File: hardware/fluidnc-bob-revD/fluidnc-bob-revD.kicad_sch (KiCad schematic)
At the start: 69 parts, among them J1 36V-IN, J10 RELAY, J11 AUX, J12 5V-EXT, J13 SD, J2 X-DRV, J3 Y-DRV, J4 Z-DRV, J5 LIM-X, J6 LIM-Y, J7 LIM-Z, J8 PROBE, J9 E-STOP, Q1 MMBT2222A, Q2 MMBT2222A, U1 SN74AHCT541N, U2 TSR 1-4850WI

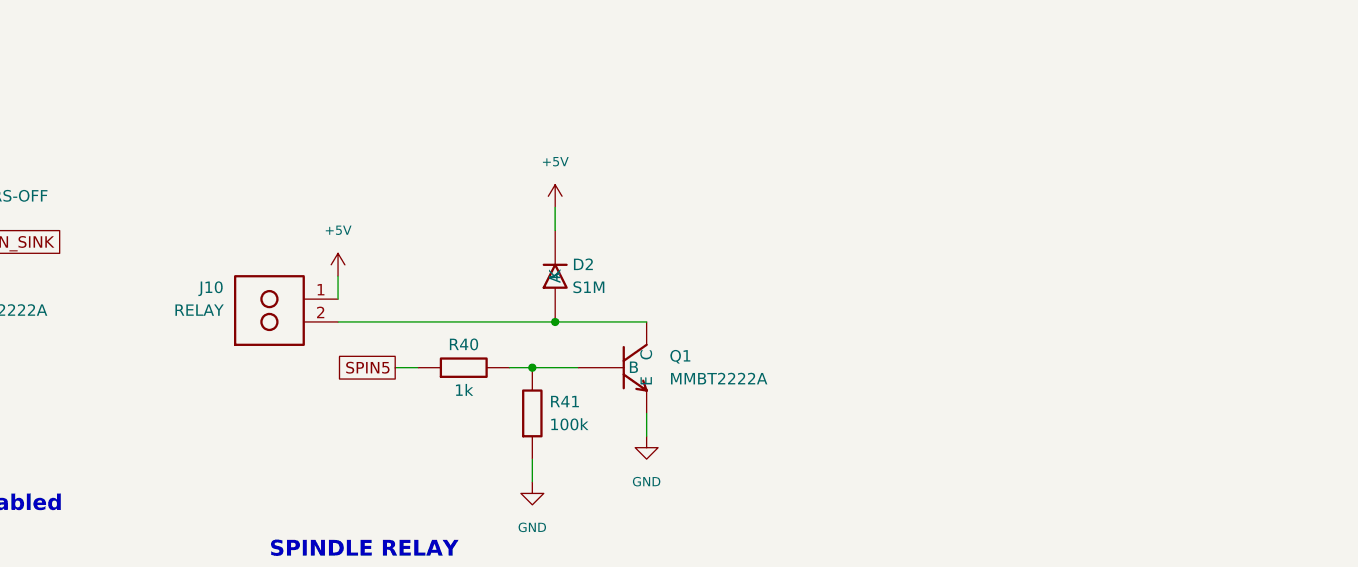
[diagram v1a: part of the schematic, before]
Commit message: hardware: rev D — onboard spindle relay (Omron G5LE-14 DC5)
Replaces the harvest-a-Songle off-board plan: G5LE-14 DC5 (SPDT,
10A/250VAC, 5V coil, DK Z1011-ND) driven by the existing Q1 low-side
sink + S1M flyback. Contacts COM/NO/NC to a 3-pos MKDS terminal (J10,
Phoenix 1715734) switching the spindle AC line — wire through NO so a
dead board fails spindle-off. Pin map (coil 2&5, COM 1, NO 3, NC 4)
decoded from the Omron datasheet + KiCad curated footprint.

verify_netlist caught a COM-to-NO short in the first contact routing
(polyline vertex landing on a terminal pin tip) — rerouted on distinct
lanes. ERC 0 violations; netlist verified. BOM/CSV/README updated,
mains creepage rules added to the layout checklist.

Co-Authored-By: Claude Fable 5 <noreply@anthropic.com>
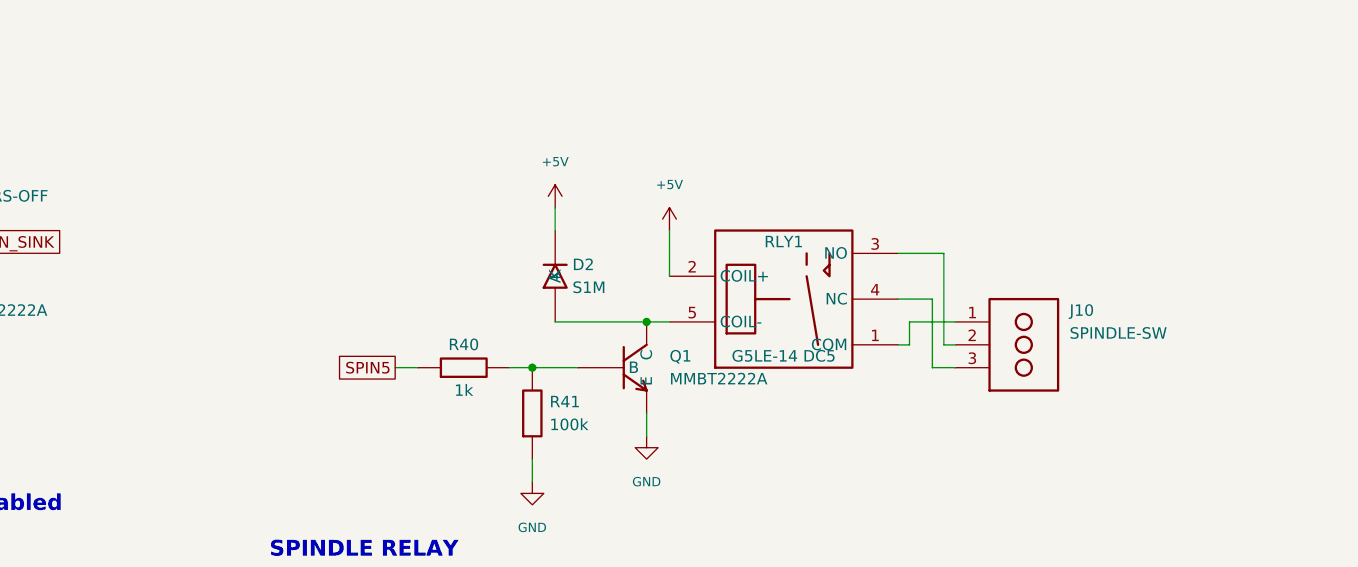
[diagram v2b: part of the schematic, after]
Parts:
- removed J10: RELAY, TerminalBlock_Phoenix:TerminalBlock_Phoenix_MKDS-1,5-2-5.08_1x02_P5.08mm_Horizontal, symbol bobD:TB_02
- added J10: SPINDLE-SW, TerminalBlock_Phoenix:TerminalBlock_Phoenix_MKDS-1,5-3-5.08_1x03_P5.08mm_Horizontal, symbol bobD:TB_03L
- added RLY1: G5LE-14 DC5, Relay_THT:Relay_SPDT_Omron-G5LE-1, symbol bobD:RELAY_G5LE
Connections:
- net +5V: now also RLY1.2 (COIL+)
- net at D2.2 (A), Q1.3 (C): now also RLY1.5 (COIL-)
- new net: J10.1, RLY1.1 (COM)
- new net: J10.2, RLY1.3 (NO)
- new net: J10.3, RLY1.4 (NC)
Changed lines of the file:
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@@
     (instances (project "fluidnc-bob-revD" (path "/d27f0a00-3830-5100-af6a-a93fbdba8465" (reference "D2") (unit 1))))
   )
-  (symbol (lib_id "bobD:TB_02") (at 158.75 220.98 0) (unit 1) (exclude_from_sim no) (in_bom yes) (on_board yes) (dnp no)
-    (property "Reference" "J10" (at 153.67 219.70999999999998 0) (effects (font (size 1.27 1.27)) (justify right)))
-    (property "Value" "RELAY" (at 153.67 222.25 0) (effects (font (size 1.27 1.27)) (justify right)))
-    (property "Footprint" "TerminalBlock_Phoenix:TerminalBlock_Phoenix_MKDS-1,5-2-5.08_1x02_P5.08mm_Horizontal" (at 158.75 220.98 0) (effects (font (size 1.27 1.27)) hide))
-    (property "Datasheet" "https://www.phoenixcontact.com/en-us/products/printed-circuit-board-terminal-mkds-15-2-508-1715721" (at 158.75 220.98 0) (effects (font (size 1.27 1.27)) hide))
-    (property "Digikey" "https://www.digikey.com/en/products/detail/phoenix-contact/1715721/260631" (at 158.75 220.98 0) (effects (font (size 1.27 1.27)) hide))
-    (pin "1")
+  (symbol (lib_id "bobD:RELAY_G5LE") (at 215.9 220.98 0) (unit 1) (exclude_from_sim no) (in_bom yes) (on_board yes) (dnp no)
+    (property "Reference" "RLY1" (at 215.9 214.63 0) (effects (font (size 1.27 1.27))))
+    (property "Value" "G5LE-14 DC5" (at 215.9 227.32999999999998 0) (effects (font (size 1.27 1.27))))
+    (property "Footprint" "Relay_THT:Relay_SPDT_Omron-G5LE-1" (at 215.9 220.98 0) (effects (font (size 1.27 1.27)) hide))
+    (property "Datasheet" "https://omronfs.omron.com/en_US/ecb/products/pdf/en-g5le.pdf" (at 215.9 220.98 0) (effects (font (size 1.27 1.27)) hide))
+    (property "Digikey" "https://www.digikey.com/en/products/detail/omron-electronics-inc-emc-div/G5LE-14-DC5/280371" (at 215.9 220.98 0) (effects (font (size 1.27 1.27)) hide))
     (pin "2")
+    (pin "5")
+    (pin "1")
+    (pin "3")
+    (pin "4")
+    (instances (project "fluidnc-bob-revD" (path "/d27f0a00-3830-5100-af6a-a93fbdba8465" (reference "RLY1") (unit 1))))
+  )
+  (symbol (lib_id "bobD:TB_03L") (at 242.57 223.52 0) (unit 1) (exclude_from_sim no) (in_bom yes) (on_board yes) (dnp no)
+    (property "Reference" "J10" (at 247.65 222.25 0) (effects (font (size 1.27 1.27)) (justify left)))
+    (property "Value" "SPINDLE-SW" (at 247.65 224.79000000000002 0) (effects (font (size 1.27 1.27)) (justify left)))
+    (property "Footprint" "TerminalBlock_Phoenix:TerminalBlock_Phoenix_MKDS-1,5-3-5.08_1x03_P5.08mm_Horizontal" (at 242.57 223.52 0) (effects (font (size 1.27 1.27)) hide))
+    (property "Datasheet" "https://www.phoenixcontact.com/en-us/products/printed-circuit-board-terminal-mkds-15-3-508-1715734" (at 242.57 223.52 0) (effects (font (size 1.27 1.27)) hide))
+    (property "Digikey" "https://www.digikey.com/en/products/result?keywords=1715734" (at 242.57 223.52 0) (effects (font (size 1.27 1.27)) hide))
+    (pin "1")
+    (pin "2")
+    (pin "3")
     (instances (project "fluidnc-bob-revD" (path "/d27f0a00-3830-5100-af6a-a93fbdba8465" (reference "J10") (unit 1))))
   )
@@
     (instances (project "fluidnc-bob-revD" (path "/d27f0a00-3830-5100-af6a-a93fbdba8465" (reference "#PWR034") (unit 1))))
   )
-  (symbol (lib_id "power:+5V") (at 166.37 218.44 0) (unit 1) (exclude_from_sim no) (in_bom no) (on_board yes) (dnp no)
-    (property "Reference" "#PWR035" (at 166.37 218.44 0) (effects (font (size 1.27 1.27)) hide))
-    (property "Value" "+5V" (at 166.37 213.35999999999999 0) (effects (font (size 1.02 1.02))))
-    (property "Footprint" "" (at 166.37 218.44 0) (effects (font (size 1.27 1.27)) hide))
-    (property "Datasheet" "" (at 166.37 218.44 0) (effects (font (size 1.27 1.27)) hide))
-    (pin "1")
-    (instances (project "fluidnc-bob-revD" (path "/d27f0a00-3830-5100-af6a-a93fbdba8465" (reference "#PWR035") (unit 1))))
-  )
   (symbol (lib_id "power:+5V") (at 190.5 210.82 0) (unit 1) (exclude_from_sim no) (in_bom no) (on_board yes) (dnp no)
-    (property "Reference" "#PWR036" (at 190.5 210.82 0) (effects (font (size 1.27 1.27)) hide))
+    (property "Reference" "#PWR035" (at 190.5 210.82 0) (effects (font (size 1.27 1.27)) hide))
     (property "Value" "+5V" (at 190.5 205.73999999999998 0) (effects (font (size 1.02 1.02))))
     (property "Footprint" "" (at 190.5 210.82 0) (effects (font (size 1.27 1.27)) hide))
     (property "Datasheet" "" (at 190.5 210.82 0) (effects (font (size 1.27 1.27)) hide))
+    (pin "1")
+    (instances (project "fluidnc-bob-revD" (path "/d27f0a00-3830-5100-af6a-a93fbdba8465" (reference "#PWR035") (unit 1))))
+  )
+  (symbol (lib_id "power:+5V") (at 203.2 213.36 0) (unit 1) (exclude_from_sim no) (in_bom no) (on_board yes) (dnp no)
+    (property "Reference" "#PWR036" (at 203.2 213.36 0) (effects (font (size 1.27 1.27)) hide))
+    (property "Value" "+5V" (at 203.2 208.28 0) (effects (font (size 1.02 1.02))))
+    (property "Footprint" "" (at 203.2 213.36 0) (effects (font (size 1.27 1.27)) hide))
+    (property "Datasheet" "" (at 203.2 213.36 0) (effects (font (size 1.27 1.27)) hide))
     (pin "1")
     (instances (project "fluidnc-bob-revD" (path "/d27f0a00-3830-5100-af6a-a93fbdba8465" (reference "#PWR036") (unit 1))))
@@
   (wire (pts (xy 187.96 238.76) (xy 187.96 241.3)) (stroke (width 0) (type default)))
   (wire (pts (xy 200.66 233.68) (xy 200.66 236.22)) (stroke (width 0) (type default)))
-  (wire (pts (xy 166.37 220.98) (xy 166.37 218.44)) (stroke (width 0) (type default)))
-  (wire (pts (xy 166.37 223.52) (xy 200.66 223.52)) (stroke (width 0) (type default)))
+  (wire (pts (xy 190.5 223.52) (xy 200.66 223.52)) (stroke (width 0) (type default)))
+  (wire (pts (xy 200.66 223.52) (xy 203.2 223.52)) (stroke (width 0) (type default)))
   (wire (pts (xy 190.5 213.36) (xy 190.5 210.82)) (stroke (width 0) (type default)))
+  (wire (pts (xy 203.2 218.44) (xy 203.2 215.9)) (stroke (width 0) (type default)))
+  (wire (pts (xy 203.2 215.9) (xy 203.2 213.36)) (stroke (width 0) (type default)))
+  (wire (pts (xy 228.6 226.06) (xy 229.87 226.06)) (stroke (width 0) (type default)))
+  (wire (pts (xy 229.87 226.06) (xy 229.87 223.52)) (stroke (width 0) (type default)))
+  (wire (pts (xy 229.87 223.52) (xy 234.95 223.52)) (stroke (width 0) (type default)))
+  (wire (pts (xy 228.6 215.9) (xy 233.68 215.9)) (stroke (width 0) (type default)))
+  (wire (pts (xy 233.68 215.9) (xy 233.68 226.06)) (stroke (width 0) (type default)))
+  (wire (pts (xy 233.68 226.06) (xy 234.95 226.06)) (stroke (width 0) (type default)))
+  (wire (pts (xy 228.6 220.98) (xy 232.41 220.98)) (stroke (width 0) (type default)))
+  (wire (pts (xy 232.41 220.98) (xy 232.41 228.6)) (stroke (width 0) (type default)))
+  (wire (pts (xy 232.41 228.6) (xy 234.95 228.6)) (stroke (width 0) (type default)))
   (wire (pts (xy 312.42 167.64) (xy 309.88 167.64)) (stroke (width 0) (type default)))
   (wire (pts (xy 322.58 167.64) (xy 360.68 167.64)) (stroke (width 0) (type default)))
@@
   (junction (at 120.65 214.63) (diameter 0) (color 0 0 0 0))
   (junction (at 187.96 228.6) (diameter 0) (color 0 0 0 0))
-  (junction (at 190.5 223.52) (diameter 0) (color 0 0 0 0))
+  (junction (at 200.66 223.52) (diameter 0) (color 0 0 0 0))
   (junction (at 330.2 167.64) (diameter 0) (color 0 0 0 0))
   (junction (at 337.82 167.64) (diameter 0) (color 0 0 0 0))

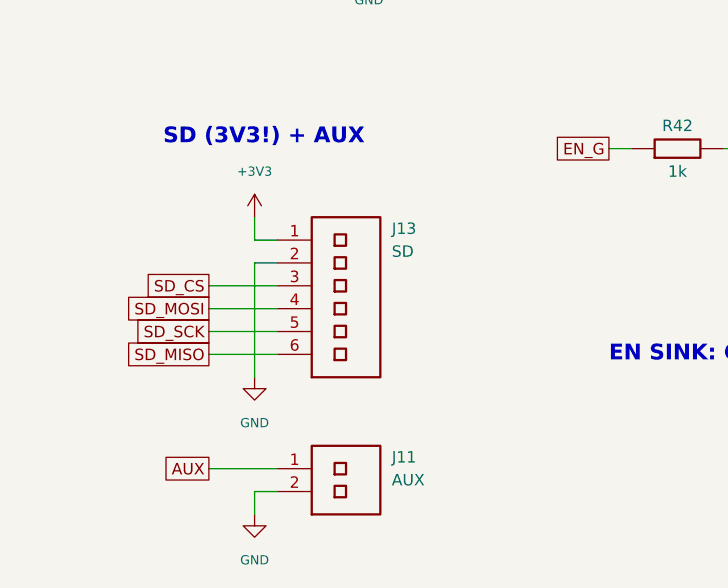
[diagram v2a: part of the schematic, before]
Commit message: hardware: rev D connectors — Molex KK-254 inputs, rev C 2x6 SD header
- J5-J9, J11: JST-XH -> Molex KK-254 (22-23-2021 header; mating
  22-01-3027 housings + 08-50-0114 crimps added to the BOM/CSV so
  cables can be made).
- J13: 6-pos XH -> 2x6 2.54mm pin header with the EXACT fabbed rev C
  pad map (5=3V3, 7=MISO, 8=MOSI, 9=SCK, 10=CS, 11/12=GND, rest NC) so
  the salvaged SD module and its cable carry over unchanged.
- ERC 0 violations; netlist verified (J13 map machine-checked).

Co-Authored-By: Claude Fable 5 <noreply@anthropic.com>
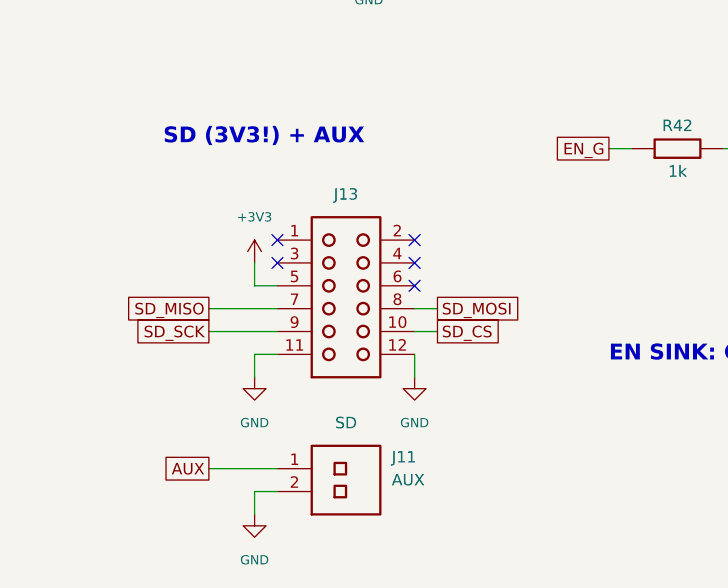
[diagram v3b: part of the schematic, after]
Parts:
- removed J11: AUX, Connector_JST:JST_XH_B2B-XH-A_1x02_P2.50mm_Vertical, symbol bobD:XH_02
- removed J13: SD, Connector_JST:JST_XH_B6B-XH-A_1x06_P2.50mm_Vertical, symbol bobD:XH_06
- removed J5: LIM-X, Connector_JST:JST_XH_B2B-XH-A_1x02_P2.50mm_Vertical, symbol bobD:XH_02
- removed J6: LIM-Y, Connector_JST:JST_XH_B2B-XH-A_1x02_P2.50mm_Vertical, symbol bobD:XH_02
- removed J7: LIM-Z, Connector_JST:JST_XH_B2B-XH-A_1x02_P2.50mm_Vertical, symbol bobD:XH_02
- removed J8: PROBE, Connector_JST:JST_XH_B2B-XH-A_1x02_P2.50mm_Vertical, symbol bobD:XH_02
- removed J9: E-STOP, Connector_JST:JST_XH_B2B-XH-A_1x02_P2.50mm_Vertical, symbol bobD:XH_02
- added J11: AUX, Connector_Molex:Molex_KK-254_AE-6410-02A_1x02_P2.54mm_Vertical, symbol bobD:KK_02
- added J13: SD, Connector_PinHeader_2.54mm:PinHeader_2x06_P2.54mm_Vertical, symbol bobD:CONN_2x6
- added J5: LIM-X, Connector_Molex:Molex_KK-254_AE-6410-02A_1x02_P2.54mm_Vertical, symbol bobD:KK_02
- added J6: LIM-Y, Connector_Molex:Molex_KK-254_AE-6410-02A_1x02_P2.54mm_Vertical, symbol bobD:KK_02
- added J7: LIM-Z, Connector_Molex:Molex_KK-254_AE-6410-02A_1x02_P2.54mm_Vertical, symbol bobD:KK_02
- added J8: PROBE, Connector_Molex:Molex_KK-254_AE-6410-02A_1x02_P2.54mm_Vertical, symbol bobD:KK_02
- added J9: E-STOP, Connector_Molex:Molex_KK-254_AE-6410-02A_1x02_P2.54mm_Vertical, symbol bobD:KK_02
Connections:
- net +3V3: now also J13.5
- net AUX: now also J11.1
- net GND: now also J11.2, J13.11, J13.12, J5.2, J6.2, J7.2, J8.2, J9.2
- net SD_CS: now also J13.10
- net SD_MISO: now also J13.7
- net SD_MOSI: now also J13.8
- net SD_SCK: now also J13.9
- net at C22.1, R22.2, R32.2: now also J7.1
- net at C21.1, R21.2, R31.2: now also J6.1
- net at C23.1, R23.2, R33.2: now also J8.1
- net at C20.1, R20.2, R30.2: now also J5.1
- net at C24.1, R24.2, R34.2: now also J9.1
- no-connect marks 20 -> 25
